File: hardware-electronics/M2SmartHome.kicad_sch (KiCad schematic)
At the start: 7 parts, among them J1 M.2-Key-M-edge-connector

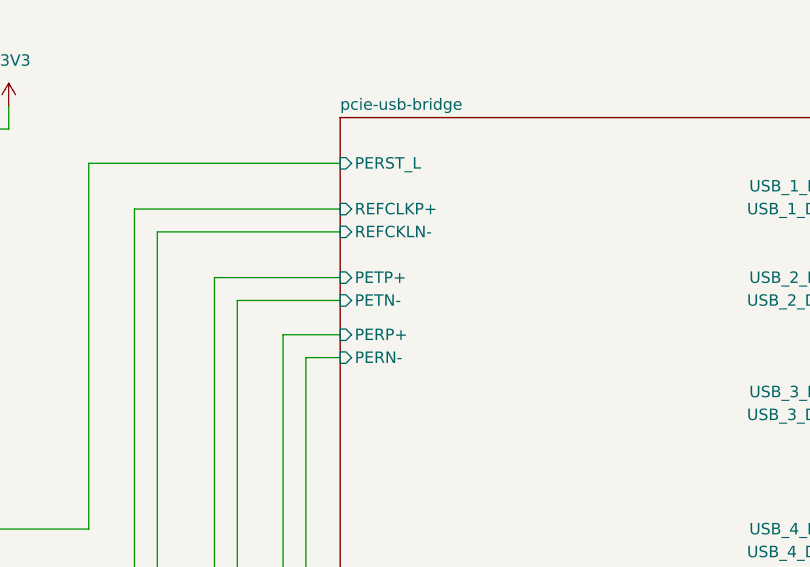
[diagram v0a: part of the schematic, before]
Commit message: [#17] PCIe WIP routing plan
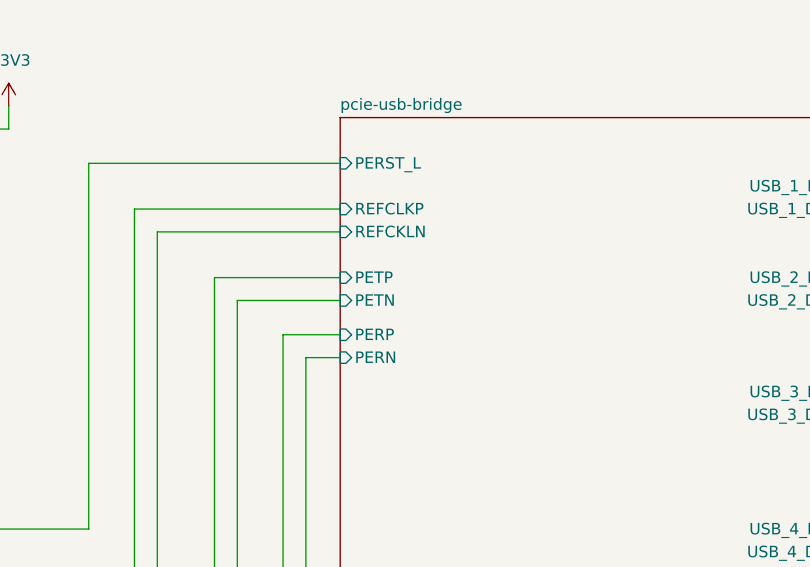
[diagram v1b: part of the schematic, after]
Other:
- sheet pcie-usb-bridge ports: added PERN, PERP, PETN, PETP, REFCKLN, REFCLKP; removed PERN-, PERP+, PETN-, PETP+, REFCKLN-, REFCLKP+
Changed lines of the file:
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@@
 			)
 		)
-		(pin "REFCLKP+" input
+		(pin "REFCLKP" input
 			(at 176.53 67.31 180)
 			(effects
@@
 			)
 		)
-		(pin "PERN-" input
+		(pin "PERN" input
 			(at 176.53 83.82 180)
 			(effects
@@
 			)
 		)
-		(pin "PETP+" input
+		(pin "PETP" input
 			(at 176.53 74.93 180)
 			(effects
@@
 			)
 		)
-		(pin "PERP+" input
+		(pin "PERP" input
 			(at 176.53 81.28 180)
 			(effects
@@
 			)
 		)
-		(pin "REFCKLN-" input
+		(pin "REFCKLN" input
 			(at 176.53 69.85 180)
 			(effects
@@
 			)
 		)
-		(pin "PETN-" input
+		(pin "PETN" input
 			(at 176.53 77.47 180)
 			(effects

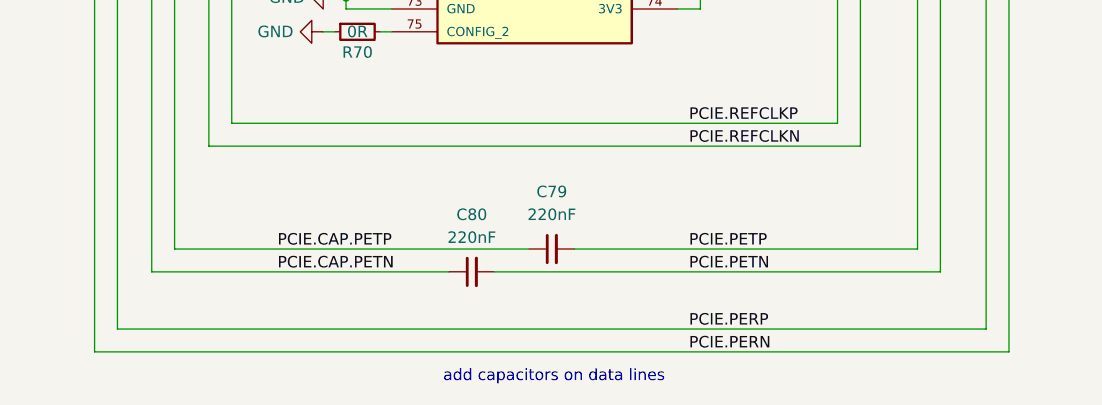
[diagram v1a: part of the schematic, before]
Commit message: [#24] SCH add PCIe connections to TUSB7340IRKMT
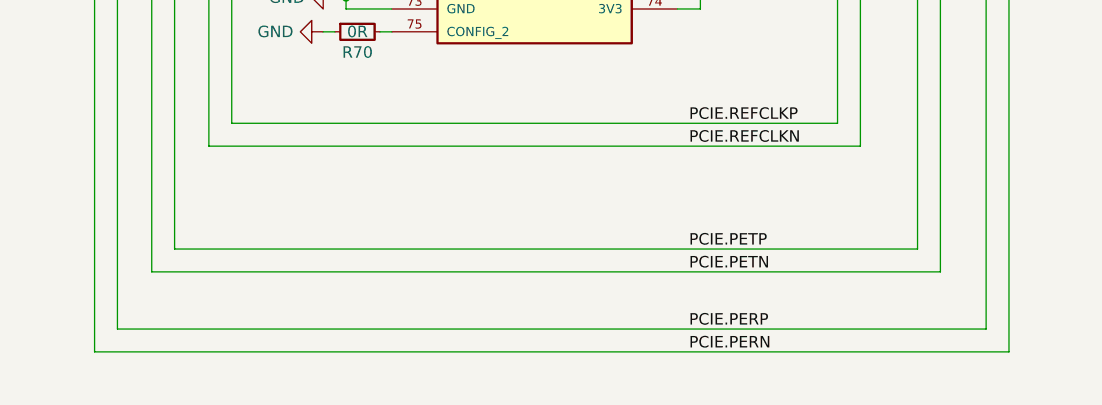
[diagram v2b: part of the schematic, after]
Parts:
- removed C79, C80: C_220nF_0402, M2SmartHomeFootprints:C_0402, symbol M2SmartHomeSymbols:C_220nF_0402
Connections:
- net PCIE.CAP.PETN is gone; now on net PCIE.PETN: J1.47 (SATA-A-/PETn0)
- net PCIE.CAP.PETP is gone; now on net PCIE.PETP: J1.49 (SATA-A+/PETp0)
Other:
- note removed: "add capacitors on data lines"

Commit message: Restore design files from commit 30c85d8
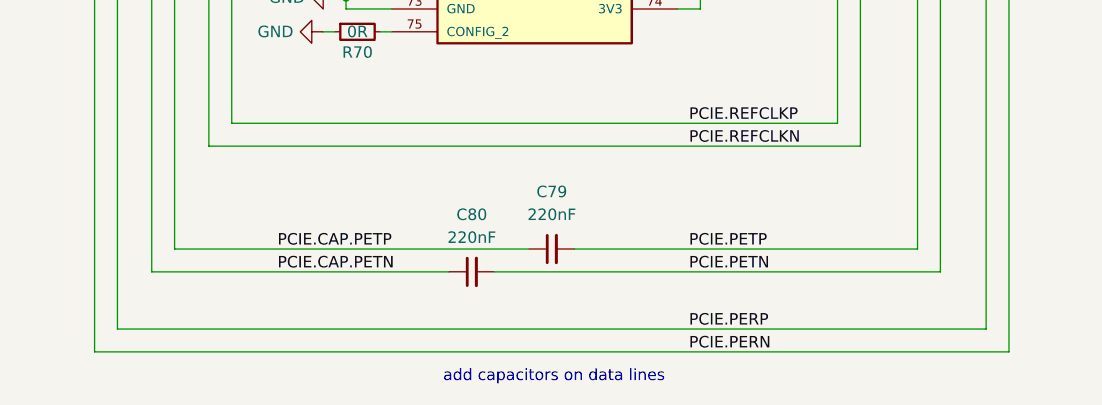
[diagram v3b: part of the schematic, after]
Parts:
- added C79, C80: C_220nF_0402, M2SmartHomeFootprints:C_0402, symbol M2SmartHomeSymbols:C_220nF_0402
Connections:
- net PCIE.PETN: now also C80.2; no longer J1.47 (SATA-A-/PETn0)
- net PCIE.PETP: now also C79.2; no longer J1.49 (SATA-A+/PETp0)
- new net PCIE.CAP.PETN: C80.1, J1.47 (SATA-A-/PETn0)
- new net PCIE.CAP.PETP: C79.1, J1.49 (SATA-A+/PETp0)
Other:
- note added: "add capacitors on data lines"

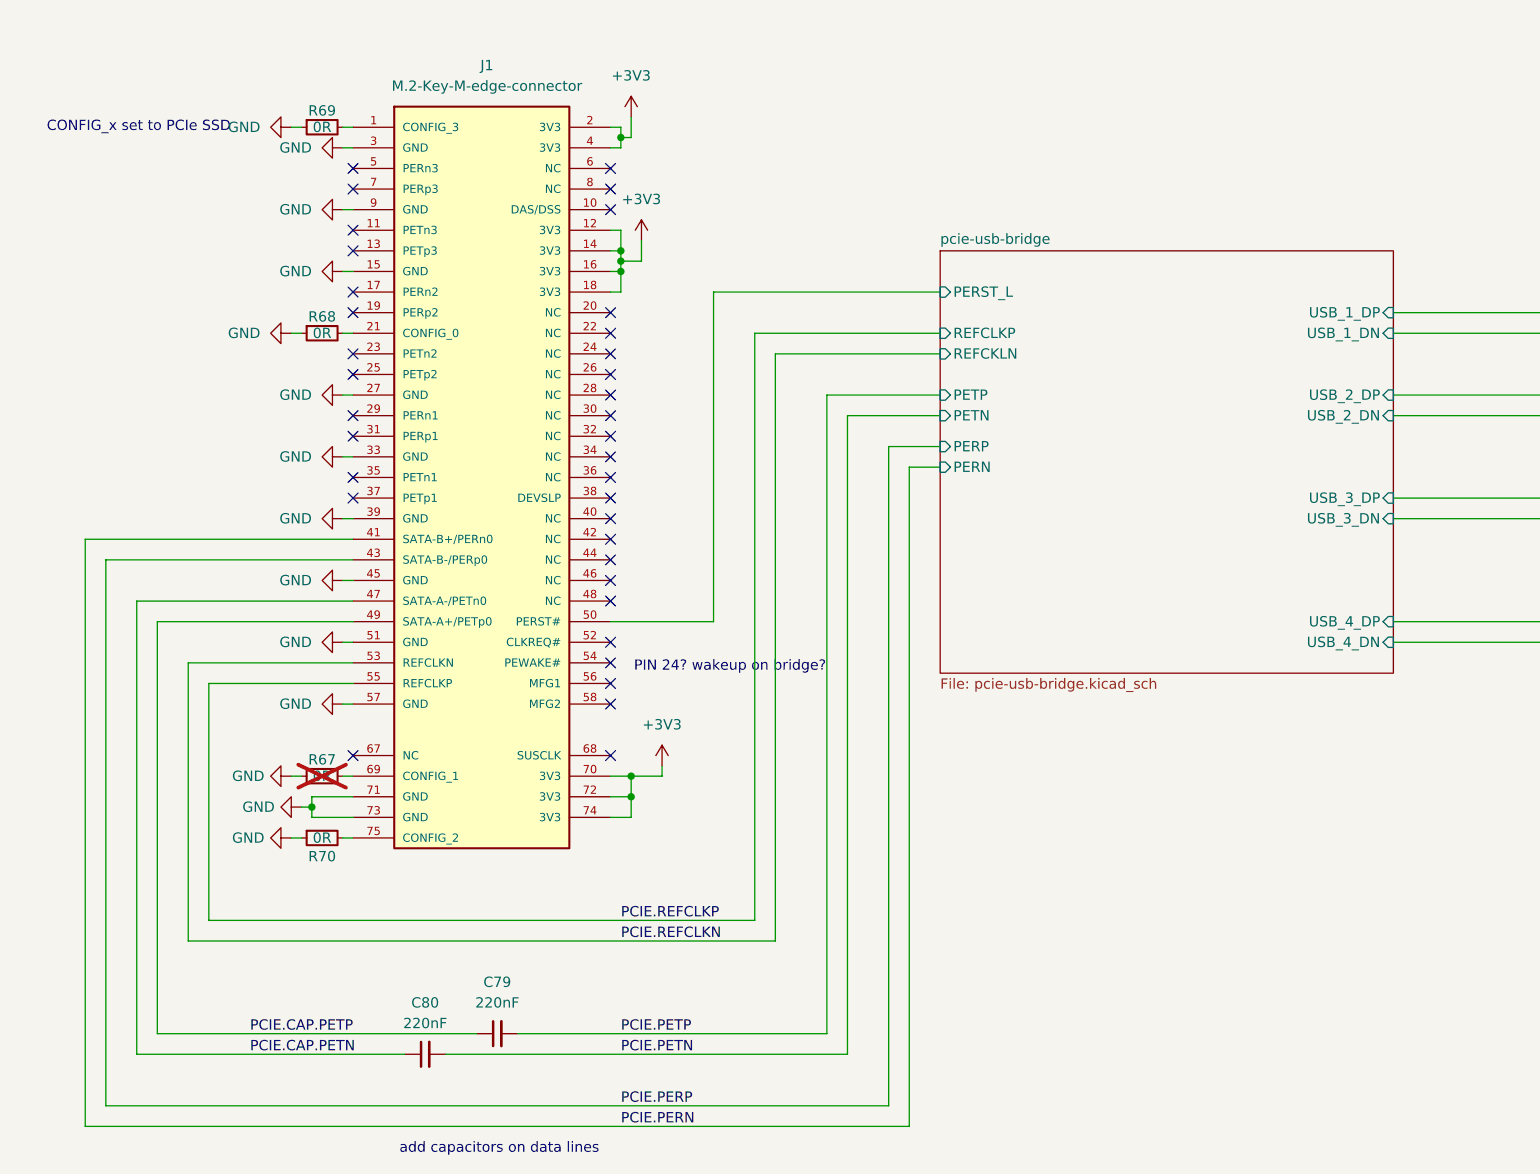
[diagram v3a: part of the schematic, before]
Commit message: [#24] SCH Pcie bridge WAKE and CLKREQ signals
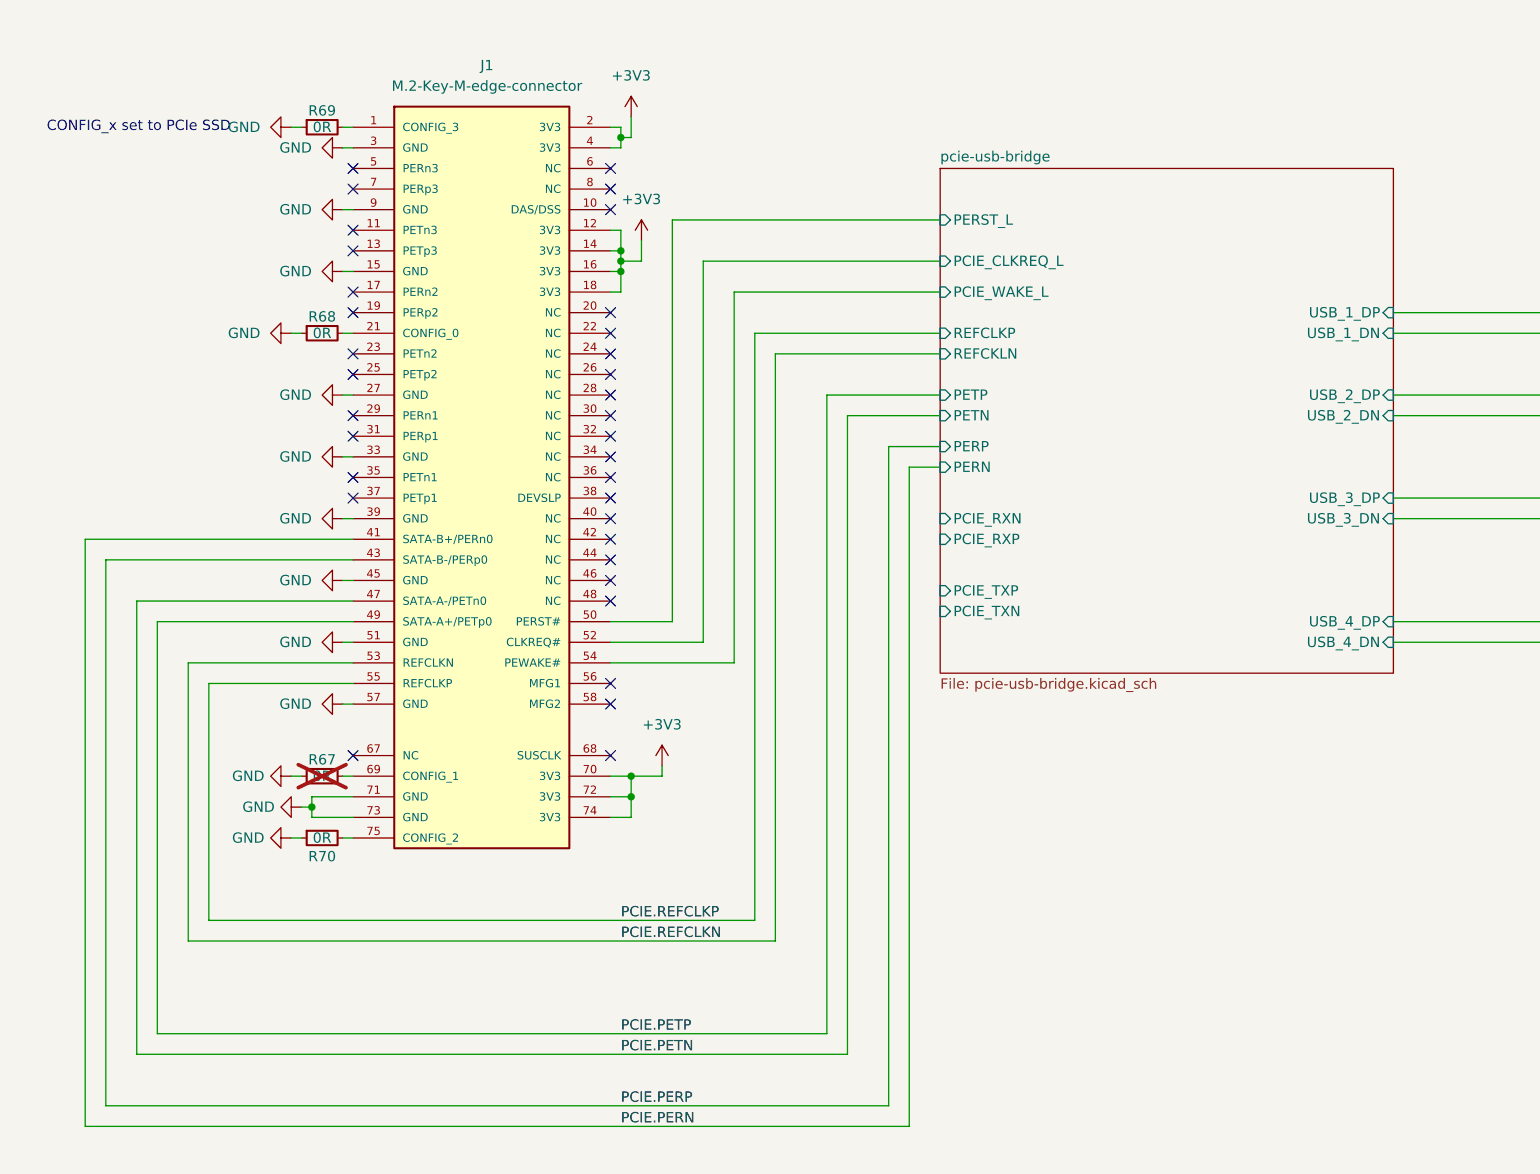
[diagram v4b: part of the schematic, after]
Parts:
- removed C79, C80: C_220nF_0402, M2SmartHomeFootprints:C_0402, symbol M2SmartHomeSymbols:C_220nF_0402
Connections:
- net PCIE.CAP.PETN is gone; now on net PCIE.PETN: J1.47 (SATA-A-/PETn0)
- net PCIE.CAP.PETP is gone; now on net PCIE.PETP: J1.49 (SATA-A+/PETp0)
- net pcie-usb-bridge/PCIE_CLKREQ_L: now reaches J1.52 (CLKREQ#)
- net pcie-usb-bridge/PCIE_WAKE_L: now reaches J1.54 (PEWAKE#)
- no-connect marks 36 -> 34
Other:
- sheet pcie-usb-bridge ports: added PCIE_CLKREQ_L, PCIE_RXN, PCIE_RXP, PCIE_TXN, PCIE_TXP, PCIE_WAKE_L; removed none
- note removed: "PIN 24? wakeup on bridge?"
- note removed: "add capacitors on data lines"

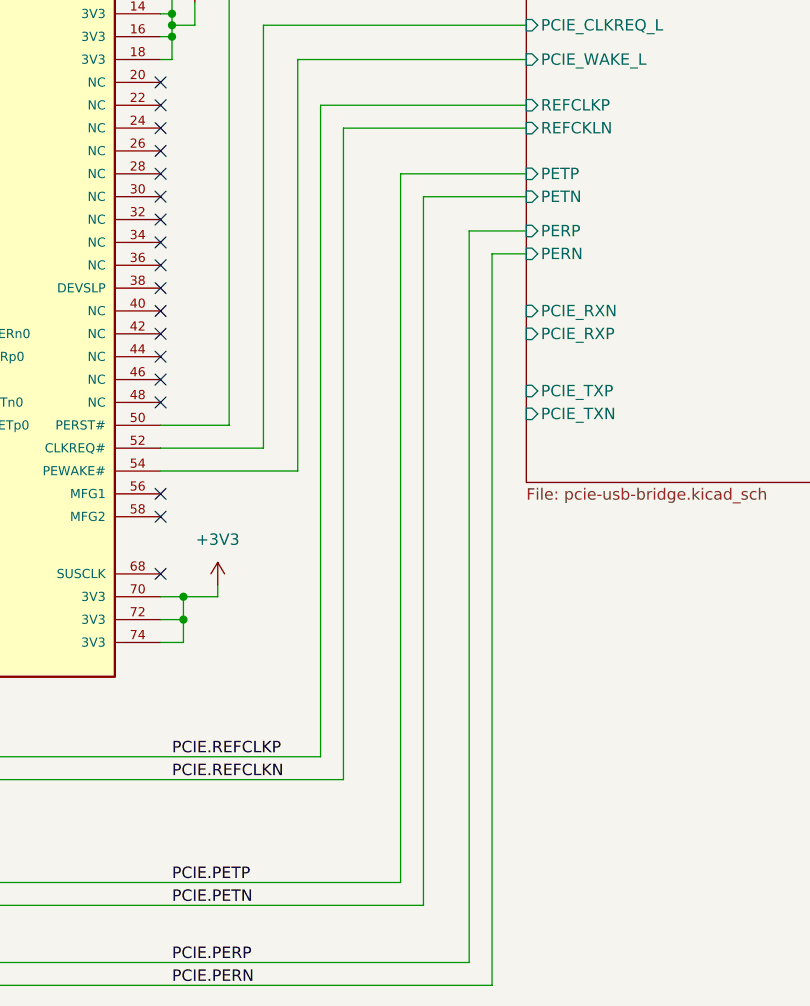
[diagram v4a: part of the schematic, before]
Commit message: [#24] PCB Pcie bridge placement WIP
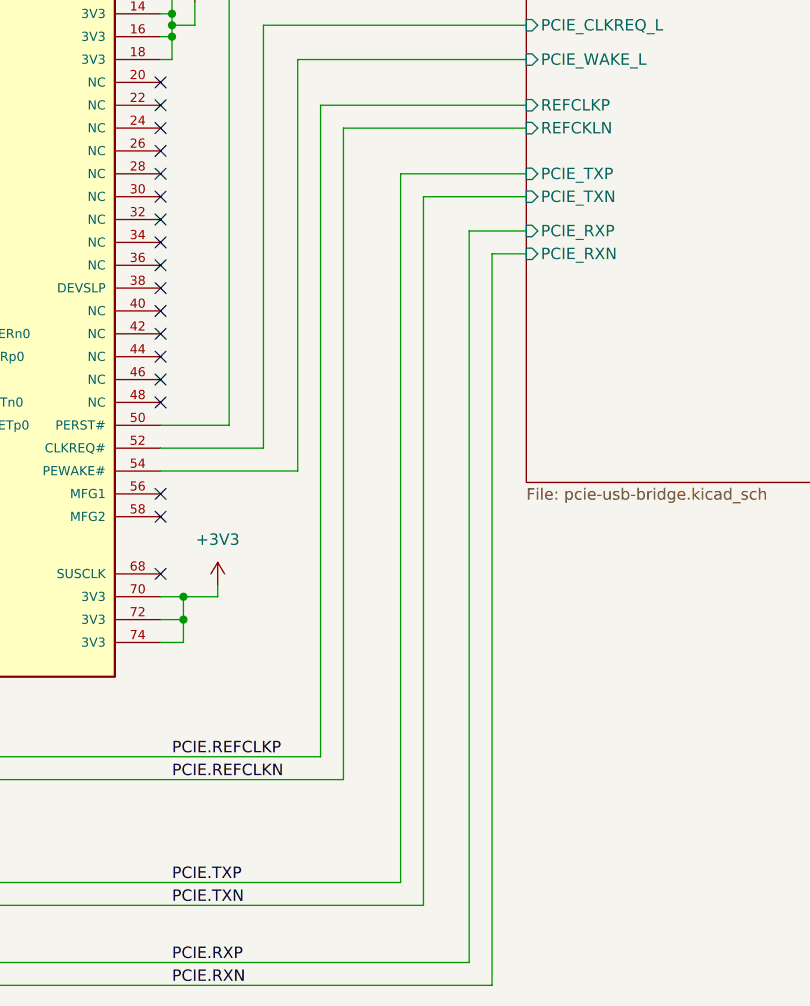
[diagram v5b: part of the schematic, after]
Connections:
- net PCIE.PERN renamed PCIE.RXN
- net PCIE.PERP renamed PCIE.RXP
- net PCIE.PETN renamed PCIE.TXN
- net PCIE.PETP renamed PCIE.TXP
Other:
- sheet pcie-usb-bridge ports: added none; removed PERN, PERP, PETN, PETP
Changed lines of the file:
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@@
 		)
 	)
-	(label "PCIE.PETN"
+	(label "PCIE.TXN"
 		(at 137.16 156.21 0)
 		(fields_autoplaced yes)
@@
 		)
 	)
-	(label "PCIE.PERN"
+	(label "PCIE.RXN"
 		(at 137.16 165.1 0)
 		(fields_autoplaced yes)
@@
 		)
 	)
-	(label "PCIE.PERP"
+	(label "PCIE.RXP"
 		(at 137.16 162.56 0)
 		(fields_autoplaced yes)
@@
 		)
 	)
-	(label "PCIE.PETP"
+	(label "PCIE.TXP"
 		(at 137.16 153.67 0)
 		(fields_autoplaced yes)
@@
 			)
 		)
-		(pin "PERN" input
-			(at 176.53 83.82 180)
-			(effects
-				(font
-					(size 1.27 1.27)
-				)
-				(justify left)
-			)
-		)
-		(pin "PETP" input
-			(at 176.53 74.93 180)
-			(effects
-				(font
-					(size 1.27 1.27)
-				)
-				(justify left)
-			)
-		)
-		(pin "PERP" input
-			(at 176.53 81.28 180)
-			(effects
-				(font
-					(size 1.27 1.27)
-				)
-				(justify left)
-			)
-		)
 		(pin "REFCKLN" input
 			(at 176.53 69.85 180)
@@
 			)
 		)
-		(pin "PETN" input
-			(at 176.53 77.47 180)
-			(effects
-				(font
-					(size 1.27 1.27)
-				)
-				(justify left)
-			)
-		)
 		(pin "PCIE_WAKE_L" input
 			(at 176.53 62.23 180)
@@
 		)
 		(pin "PCIE_RXN" input
-			(at 176.53 90.17 180)
+			(at 176.53 83.82 180)
 			(effects
 				(font
@@
 		)
 		(pin "PCIE_RXP" input
-			(at 176.53 92.71 180)
+			(at 176.53 81.28 180)
 			(effects
 				(font
@@
 		)
 		(pin "PCIE_TXP" input
-			(at 176.53 99.06 180)
+			(at 176.53 74.93 180)
 			(effects
 				(font
@@
 		)
 		(pin "PCIE_TXN" input
-			(at 176.53 101.6 180)
-			(effects
-				(font
+			(at 176.53 77.47 180)
+			(effects
+				(font
